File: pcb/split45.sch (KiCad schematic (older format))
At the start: 92 parts, among them U1 nice_nano, U2 nice_nano

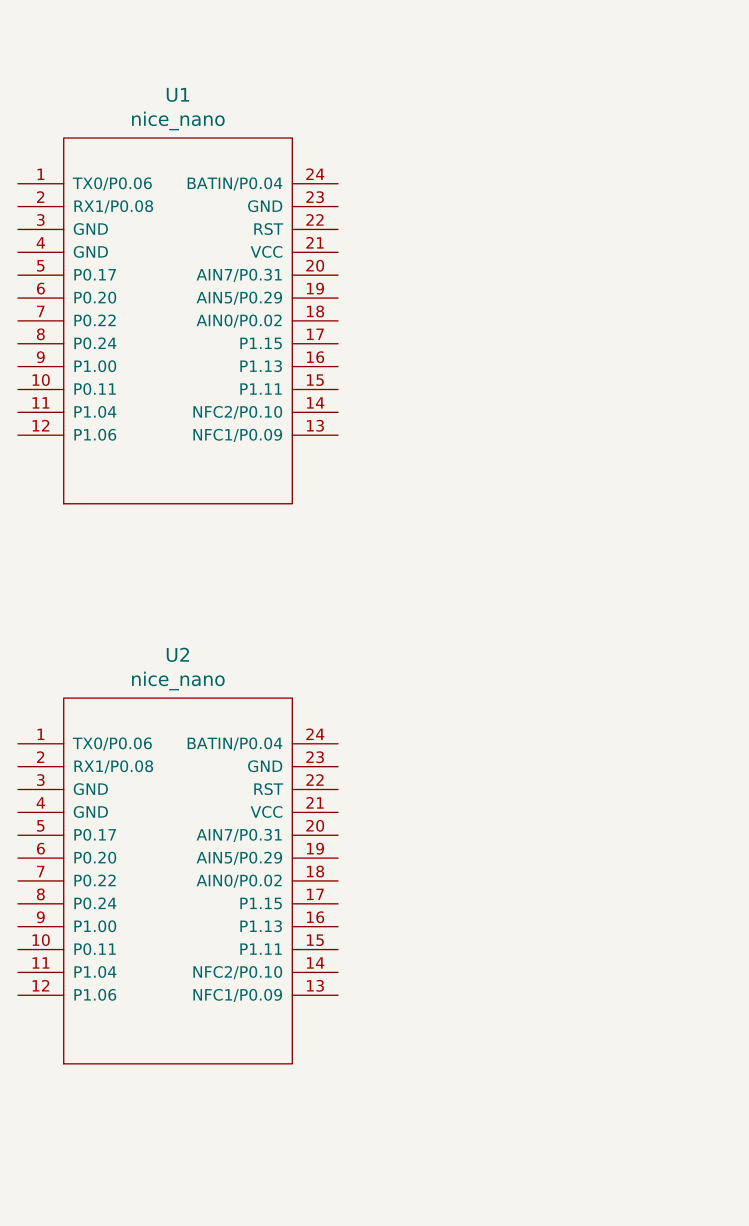
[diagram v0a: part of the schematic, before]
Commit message: route the left side
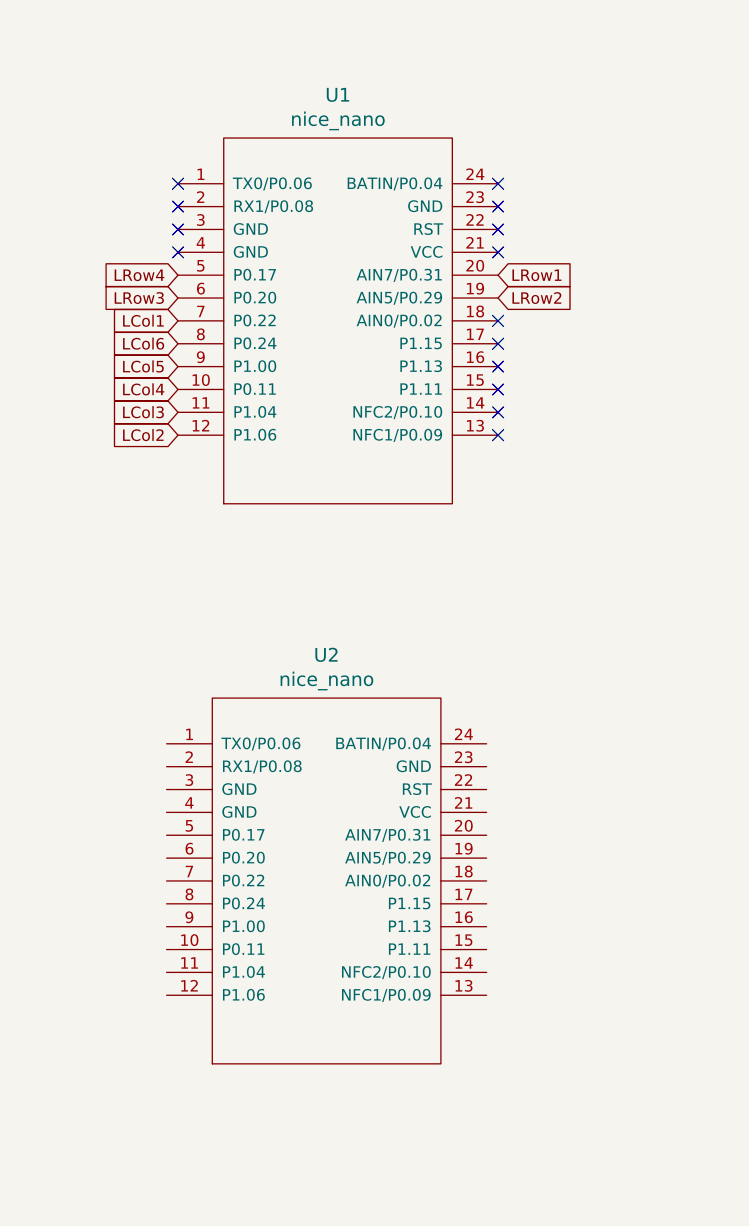
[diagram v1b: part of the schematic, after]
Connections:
- net LCol1: now also U1.7 (P0.22)
- net LCol2: now also U1.12 (P1.06)
- net LCol3: now also U1.11 (P1.04)
- net LCol4: now also U1.10 (P0.11)
- net LCol5: now also U1.9 (P1.00)
- net LCol6: now also U1.8 (P0.24)
- net LRow1: now also U1.20 (AIN7/P0.31)
- net LRow2: now also U1.19 (AIN5/P0.29)
- net LRow3: now also U1.6 (P0.20)
- net LRow4: now also U1.5 (P0.17)
- no-connect marks 0 -> 14
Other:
- moved on the sheet: U1, U2
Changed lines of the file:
@@
 	3950 9800 4950 9800
+$Comp
+L nice_nano:nice_nano U2
+U 1 1 60F4CBBD
+P 2250 4700
+F 0 "U2" H 2250 5637 60  0000 C CNN
+F 1 "nice_nano" H 2250 5531 60  0000 C CNN
+F 2 "nice-nano-kicad:nice_nano" V 3300 2200 60  0001 C CNN
+F 3 "" V 3300 2200 60  0001 C CNN
+	1    2250 4700
+	1    0    0    -1
+$EndComp
+NoConn ~ 3000 1700
+NoConn ~ 3000 1800
+NoConn ~ 3000 1900
+NoConn ~ 3000 2000
+NoConn ~ 1600 1700
+NoConn ~ 1600 1800
+NoConn ~ 1600 1900
+NoConn ~ 1600 2000
+Text GLabel 3000 2100 2    50   Input ~ 0
+LRow1
+Text GLabel 3000 2200 2    50   Input ~ 0
+LRow2
+Text GLabel 1600 2100 0    50   Input ~ 0
+LRow4
+Text GLabel 1600 2200 0    50   Input ~ 0
+LRow3
+Text GLabel 1600 2300 0    50   Input ~ 0
+LCol1
+Text GLabel 1600 2400 0    50   Input ~ 0
+LCol6
+Text GLabel 1600 2500 0    50   Input ~ 0
+LCol5
+Text GLabel 1600 2600 0    50   Input ~ 0
+LCol4
+Text GLabel 1600 2700 0    50   Input ~ 0
+LCol3
+Text GLabel 1600 2800 0    50   Input ~ 0
+LCol2
+NoConn ~ 3000 2800
+NoConn ~ 3000 2700
+NoConn ~ 3000 2600
+NoConn ~ 3000 2500
+NoConn ~ 3000 2400
+NoConn ~ 3000 2300
 $Comp
 L nice_nano:nice_nano U1
 U 1 1 60F4B577
-P 1600 2250
-F 0 "U1" H 1600 3187 60  0000 C CNN
-F 1 "nice_nano" H 1600 3081 60  0000 C CNN
-F 2 "nice-nano-kicad:nice_nano" V 2650 -250 60  0001 C CNN
-F 3 "" V 2650 -250 60  0001 C CNN
-	1    1600 2250
+P 2300 2250
+F 0 "U1" H 2300 3187 60  0000 C CNN
+F 1 "nice_nano" H 2300 3081 60  0000 C CNN
+F 2 "nice-nano-kicad:nice_nano" V 3350 -250 60  0001 C CNN
+F 3 "" V 3350 -250 60  0001 C CNN
+	1    2300 2250
 	1    0    0    -1
 $EndComp
-$Comp
-L nice_nano:nice_nano U2
-U 1 1 60F4CBBD
-P 1600 4700
-F 0 "U2" H 1600 5637 60  0000 C CNN
-F 1 "nice_nano" H 1600 5531 60  0000 C CNN
-F 2 "nice-nano-kicad:nice_nano" V 2650 2200 60  0001 C CNN
-F 3 "" V 2650 2200 60  0001 C CNN
-	1    1600 4700
-	1    0    0    -1
-$EndComp

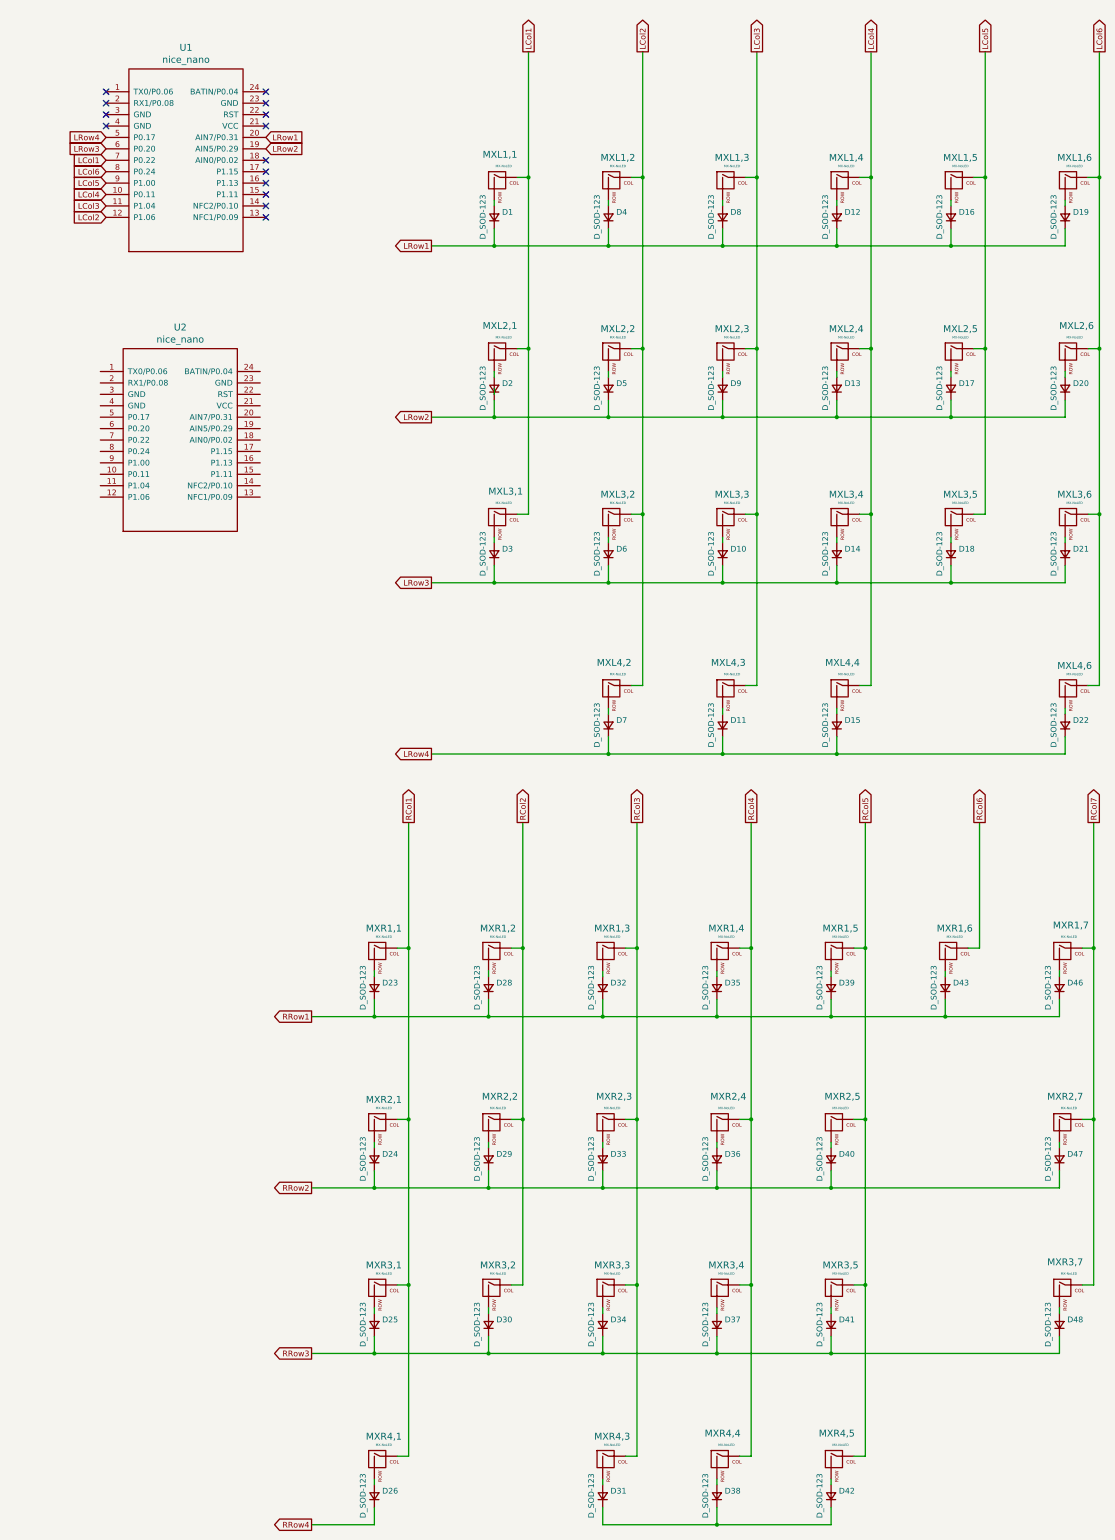
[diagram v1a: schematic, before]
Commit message: right hand routing and fill areas
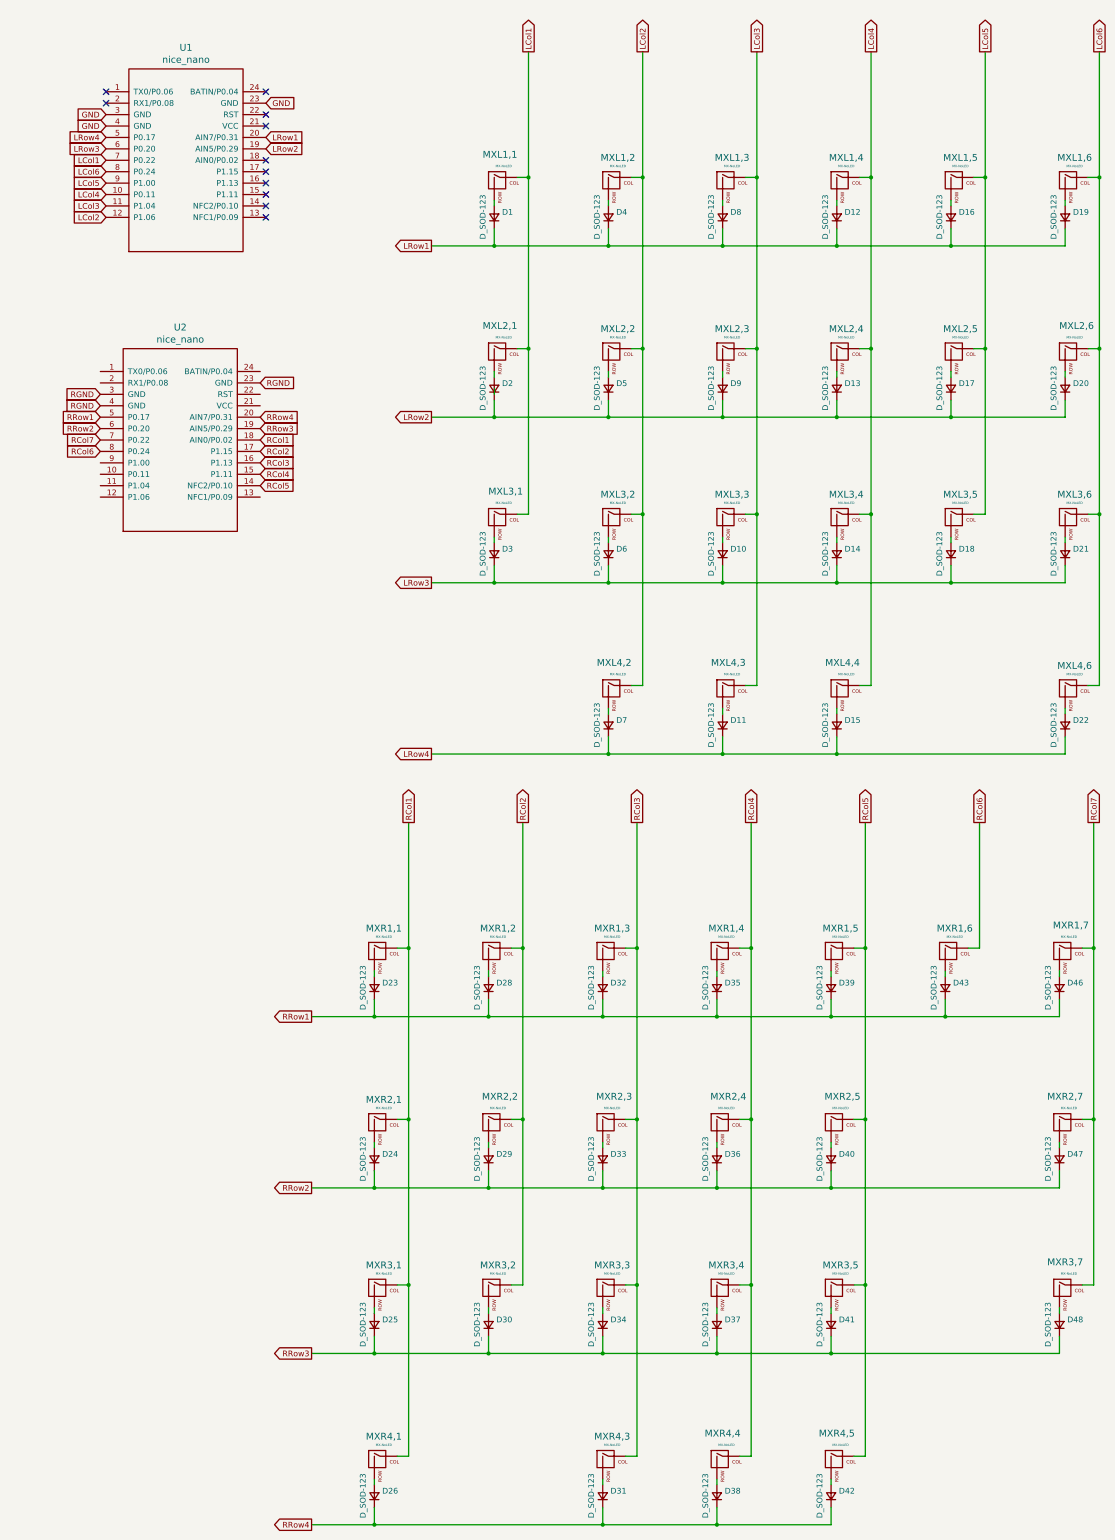
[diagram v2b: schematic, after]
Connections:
- net RCol1: now also U2.18 (AIN0/P0.02)
- net RCol2: now also U2.17 (P1.15)
- net RCol3: now also U2.16 (P1.13)
- net RCol4: now also U2.15 (P1.11)
- net RCol5: now also U2.14 (NFC2/P0.10)
- net RCol6: now also U2.8 (P0.24)
- net RCol7: now also U2.7 (P0.22)
- net RRow1: now also U2.5 (P0.17)
- net RRow2: now also U2.6 (P0.20)
- net RRow3: now also U2.19 (AIN5/P0.29)
- net RRow4: now also D31.1 (K), D38.1 (K), D42.1 (K), U2.20 (AIN7/P0.31)
- net GND: now reaches U1.23 (GND)
- net GND: now also U1.3 (GND), U1.4 (GND)
- net RGND: now reaches U2.23 (GND)
- net RGND: now also U2.3 (GND), U2.4 (GND)
- no-connect marks 14 -> 11
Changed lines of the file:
@@
 $EndComp
 NoConn ~ 3000 1700
-NoConn ~ 3000 1800
 NoConn ~ 3000 1900
 NoConn ~ 3000 2000
 NoConn ~ 1600 1700
 NoConn ~ 1600 1800
-NoConn ~ 1600 1900
-NoConn ~ 1600 2000
 Text GLabel 3000 2100 2    50   Input ~ 0
 LRow1
@@
 	1    0    0    -1
 $EndComp
+Text GLabel 3000 1800 2    50   Input ~ 0
+GND
+Text GLabel 1600 1900 0    50   Input ~ 0
+GND
+Text GLabel 1600 2000 0    50   Input ~ 0
+GND
+Wire Wire Line
+	3950 14250 5950 14250
+Connection ~ 3950 14250
+Connection ~ 5950 14250
+Text GLabel 1550 4650 0    50   Input ~ 0
+RRow2
+Text GLabel 1550 4550 0    50   Input ~ 0
+RRow1
+Text GLabel 2950 4550 2    50   Input ~ 0
+RRow4
+Text GLabel 2950 4650 2    50   Input ~ 0
+RRow3
+Text GLabel 1550 4750 0    50   Input ~ 0
+RCol7
+Text GLabel 1550 4850 0    50   Input ~ 0
+RCol6
+Text GLabel 2950 4750 2    50   Input ~ 0
+RCol1
+Text GLabel 2950 4850 2    50   Input ~ 0
+RCol2
+Text GLabel 2950 4950 2    50   Input ~ 0
+RCol3
+Text GLabel 2950 5050 2    50   Input ~ 0
+RCol4
+Text GLabel 2950 5150 2    50   Input ~ 0
+RCol5
+Text GLabel 1550 4350 0    50   Input ~ 0
+RGND
+Text GLabel 1550 4450 0    50   Input ~ 0
+RGND
+Text GLabel 2950 4250 2    50   Input ~ 0
+RGND
 $EndSCHEMATC
